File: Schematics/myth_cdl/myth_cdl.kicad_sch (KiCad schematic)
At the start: 7 parts, among them U1 74HC193, U2 74HC193, U3 74LS32, U4 74AHC244, U5 74LS08, U6 74HC04, U7 74HC02

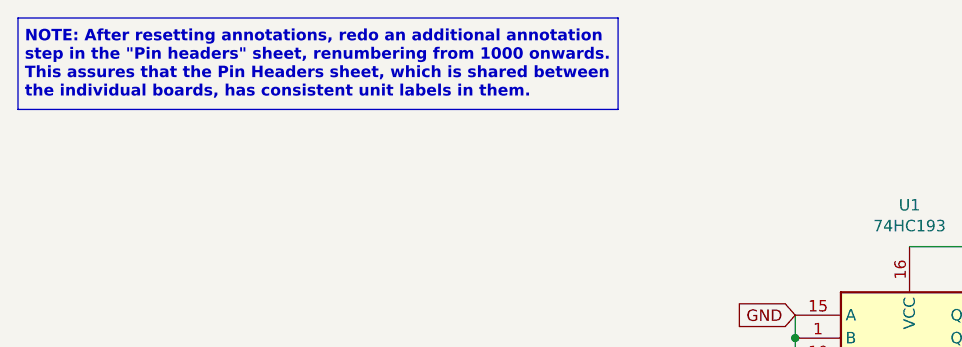
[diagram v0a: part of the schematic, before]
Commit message: Reduce number of shared headers
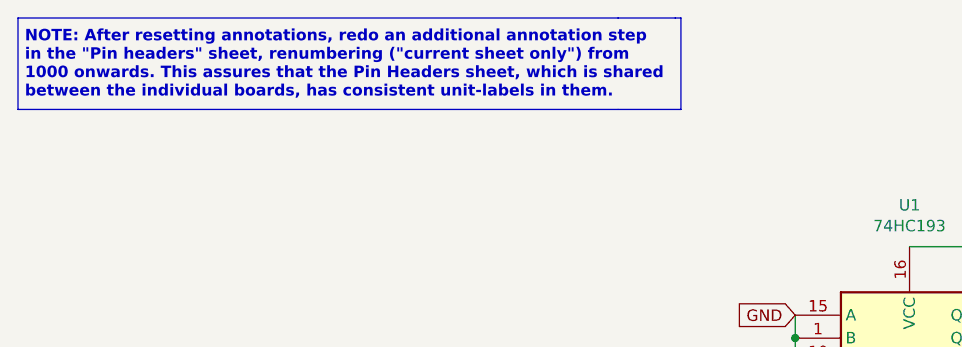
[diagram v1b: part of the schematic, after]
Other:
- note added: "NOTE: After resetting annotations, redo an additional annotation step in the "Pin headers" sheet, renumbering ("current sheet only") from 1000 onwards. This assures that the Pin Headers sheet, which is shared between the individual boards, has consistent unit-labels in them."
- note removed: "NOTE: After resetting annotations, redo an additional annotation step in the "Pin headers" sheet, renumbering from 1000 onwards. This assures that the Pin Headers sheet, which is shared between the individual boards, has consistent unit labels in them."

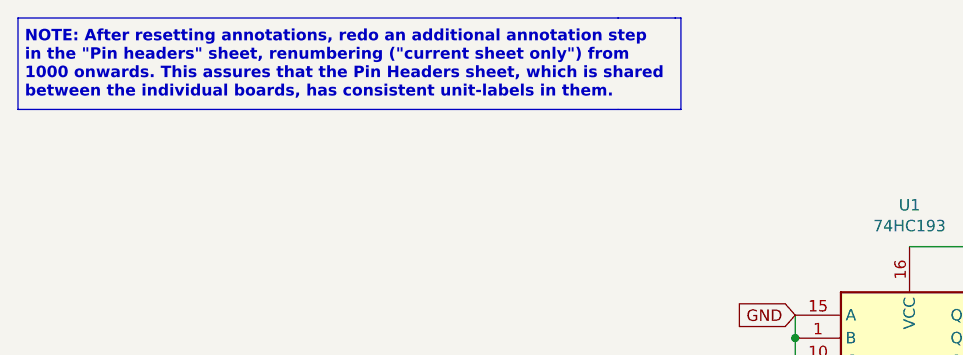
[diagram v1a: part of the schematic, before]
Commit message: Improve schematics for readability
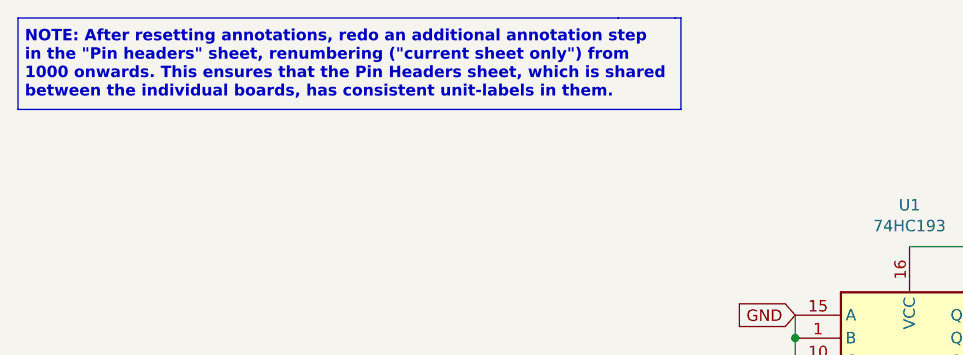
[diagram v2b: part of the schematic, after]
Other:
- note added: "NOTE: After resetting annotations, redo an additional annotation step in the "Pin headers" sheet, renumbering ("current sheet only") from 1000 onwards. This ensures that the Pin Headers sheet, which is shared between the individual boards, has consistent unit-labels in them."
- note removed: "NOTE: After resetting annotations, redo an additional annotation step in the "Pin headers" sheet, renumbering ("current sheet only") from 1000 onwards. This assures that the Pin Headers sheet, which is shared between the individual boards, has consistent unit-labels in them."
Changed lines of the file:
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@@
 		)
 	)
-	(text "NOTE: After resetting annotations, redo an additional annotation step\nin the \"Pin headers\" sheet, renumbering (\"current sheet only\") from\n1000 onwards. This assures that the Pin Headers sheet, which is shared\nbetween the individual boards, has consistent unit-labels in them."
+	(text "NOTE: After resetting annotations, redo an additional annotation step\nin the \"Pin headers\" sheet, renumbering (\"current sheet only\") from\n1000 onwards. This ensures that the Pin Headers sheet, which is shared\nbetween the individual boards, has consistent unit-labels in them."
 		(exclude_from_sim no)
 		(at 14.732 22.987 0)

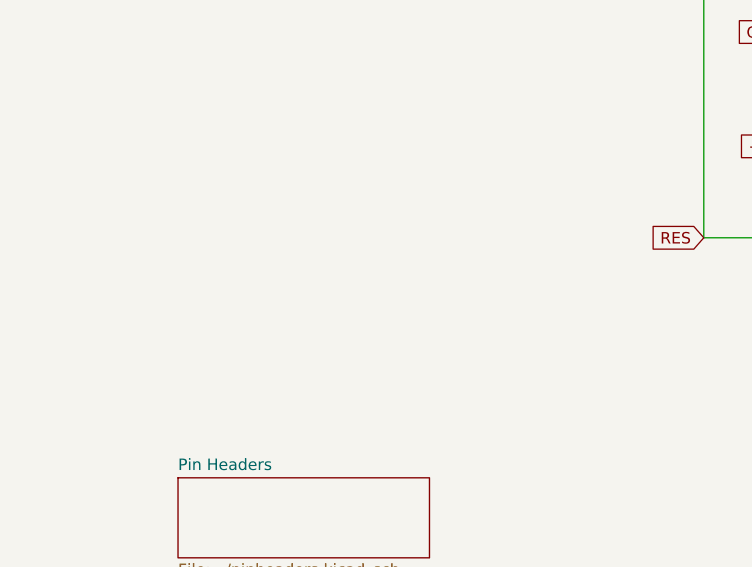
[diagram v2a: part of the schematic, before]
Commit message: Change d to g
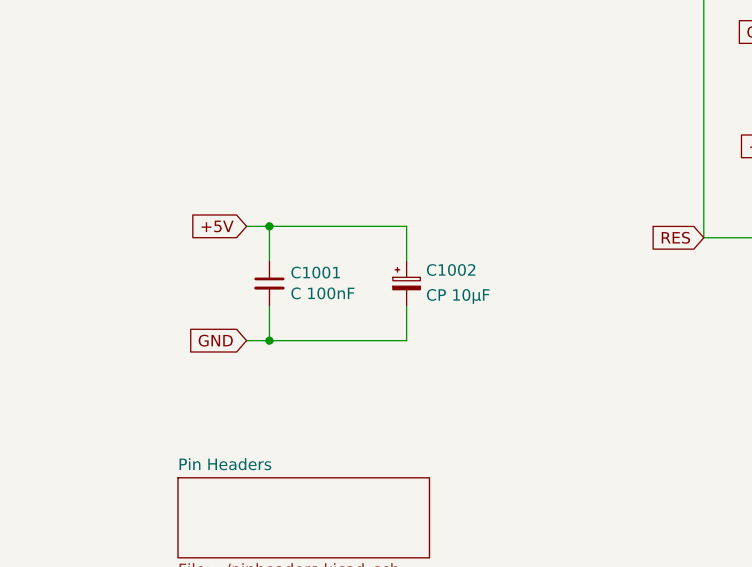
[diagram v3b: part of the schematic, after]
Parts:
- added C1001: C 100nF, Capacitor_THT:C_Disc_D5.0mm_W2.5mm_P2.50mm, symbol Device:C_Small
- added C1002: CP 10μF, Capacitor_THT:CP_Radial_D6.3mm_P2.50mm, symbol Device:C_Polarized_Small
- U3, U5, U6, U7: footprint (none) -> Package_DIP:DIP-14_W7.62mm_LongPads
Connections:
- net +5V: now also C1001.1, C1002.1
- net GND: now also C1001.2, C1002.2
